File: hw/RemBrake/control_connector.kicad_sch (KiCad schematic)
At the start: 6 parts, among them J4 Conn_01x08_MountingPin, J5 Conn_01x04_MountingPin, J6 Conn_01x03_MountingPin

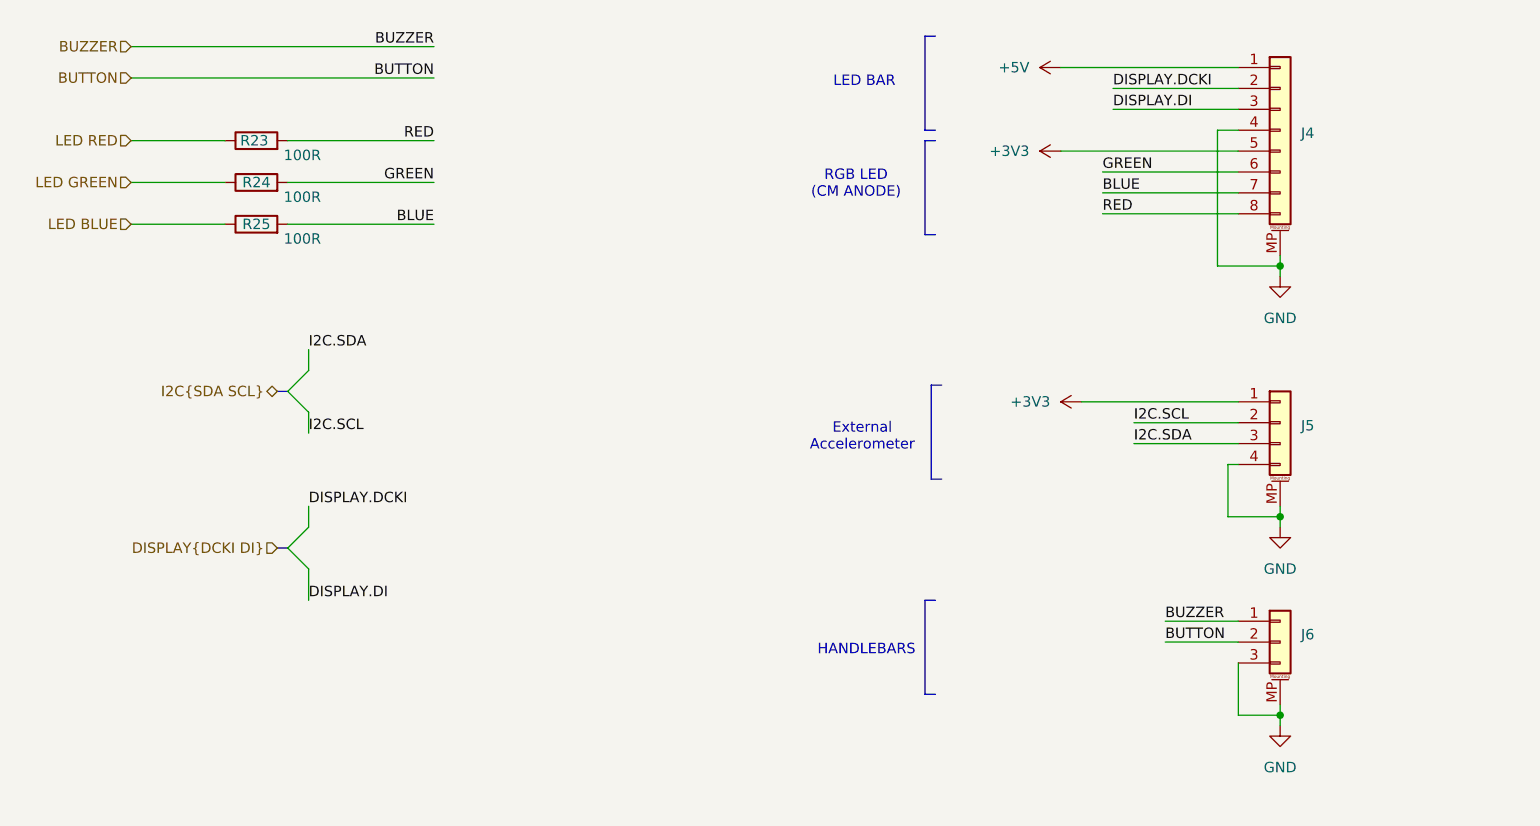
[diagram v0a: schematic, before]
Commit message: added few components to fix indicator LED undefined cathode voltage and added vbus divider to match MCU voltage level
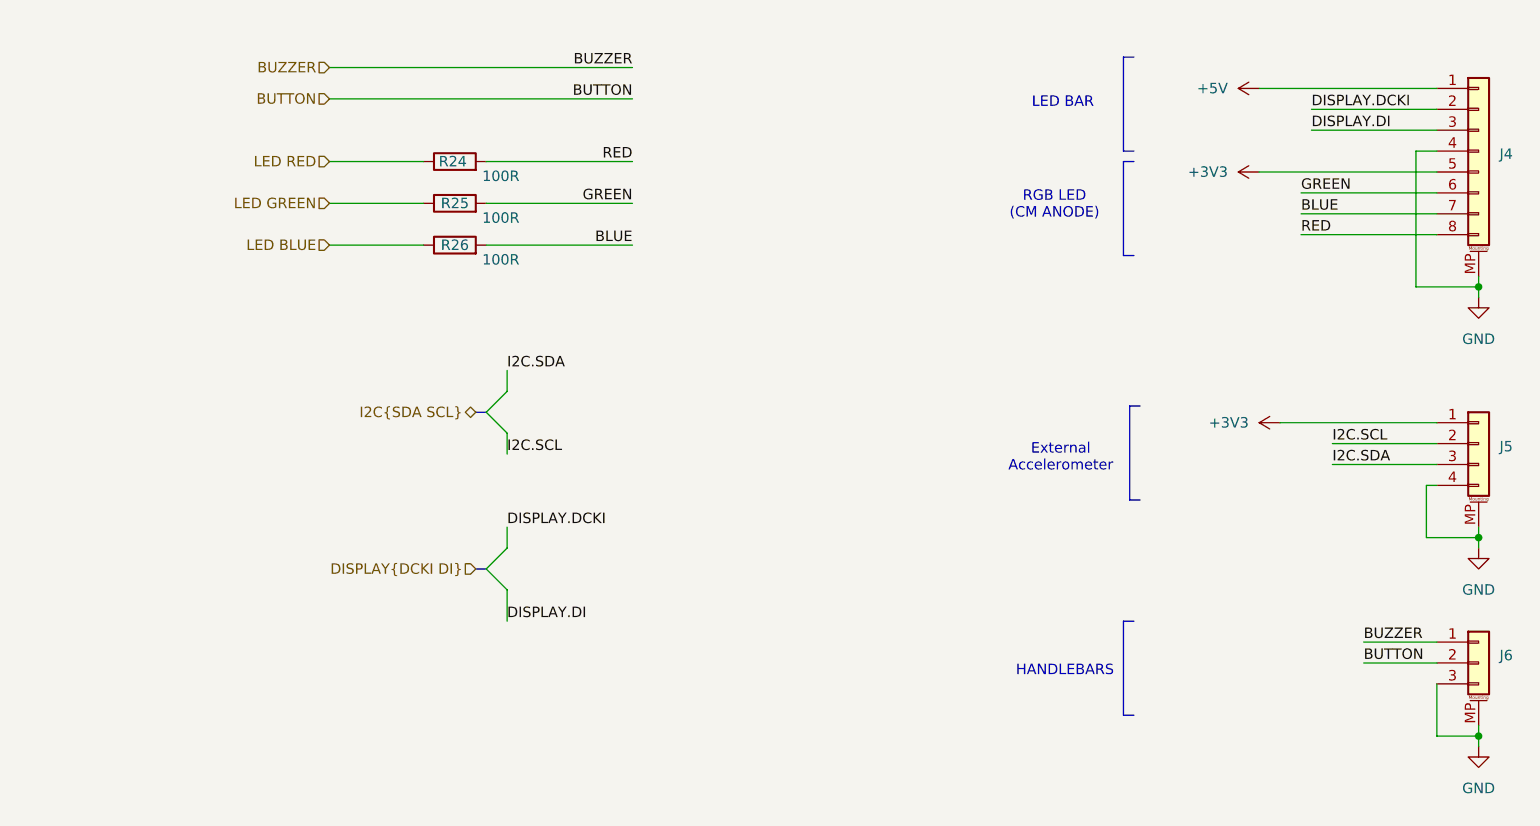
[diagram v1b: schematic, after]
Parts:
- renumbered R23 to R24, R24 to R25, R25 to R26
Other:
- moved on the sheet: J4, J5, J6, R24, R25, R26

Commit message: updated routing yet need to do some small adjustment of the polygon priorities
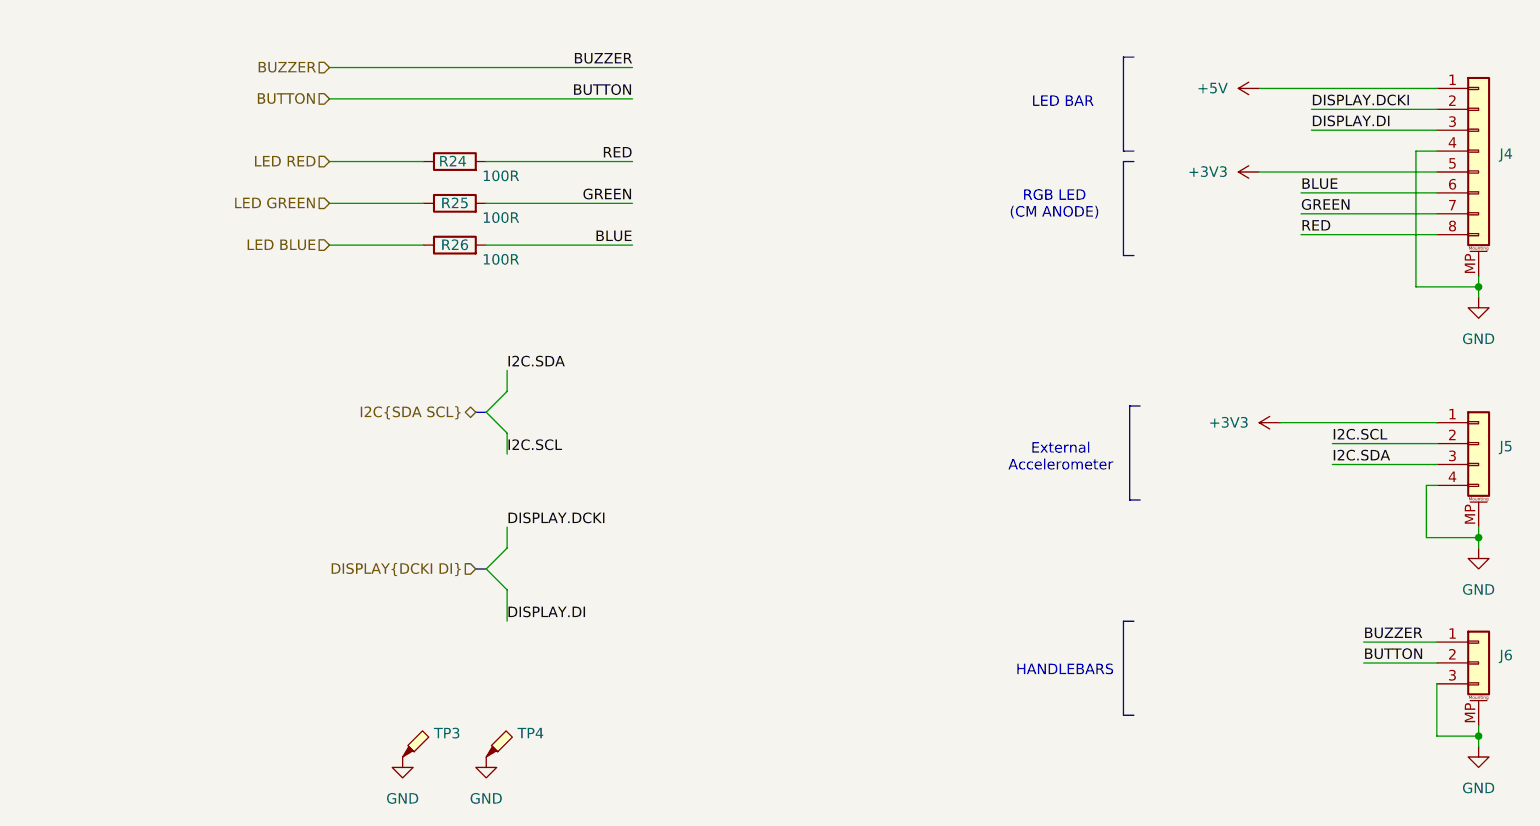
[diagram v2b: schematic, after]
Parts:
- added TP3, TP4: TestPoint_Probe, TestPoint:TestPoint_Pad_1.5x1.5mm, symbol Connector:TestPoint_Probe
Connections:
- net BLUE: now also J4.6 (Pin_6); no longer J4.7 (Pin_7)
- net GND: now also TP3.1, TP4.1
- net GREEN: now also J4.7 (Pin_7); no longer J4.6 (Pin_6)

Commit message: updated date and revision in the schematics
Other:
- company: (none) -> Pacner Bros Tech
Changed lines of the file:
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@@
 	(title_block
 		(title "Control Connector")
-		(date "2024-12-15")
-		(rev "1.0")
+		(date "2025-02-23")
+		(rev "2.0")
+		(company "Pacner Bros Tech")
 	)
 	(text "RGB LED\n(CM ANODE)\n"

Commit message: updated annotation
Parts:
- renumbered R24 to R28, R25 to R29, R26 to R30, TP3 to TP2, TP4 to TP3
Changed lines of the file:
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@@
 		(dnp no)
 		(fields_autoplaced yes)
-		(property "Reference" "#PWR062"
+		(property "Reference" "#PWR027"
 			(at 96.52 146.05 0)
 			(hide yes)
@@
 			(project "RemBrake"
 				(path "/e6d4ae5b-c9d7-4cbe-b288-c929fdf55a75/c6fda42a-9645-46e5-b66a-57cf8664dccf"
-					(reference "#PWR062")
+					(reference "#PWR027")
 					(unit 1)
 				)
@@
 		(on_board yes)
 		(dnp no)
-		(property "Reference" "R24"
+		(property "Reference" "R28"
 			(at 92.456 67.31 90)
 			(effects
@@
 		)
 		(property "Value" "100R"
-			(at 98.298 69.088 90)
+			(at 92.71 69.596 90)
 			(effects
 				(font
@@
 			(project "RemBrake"
 				(path "/e6d4ae5b-c9d7-4cbe-b288-c929fdf55a75/c6fda42a-9645-46e5-b66a-57cf8664dccf"
-					(reference "R24")
+					(reference "R28")
 					(unit 1)
 				)
@@
 		(dnp no)
 		(fields_autoplaced yes)
-		(property "Reference" "#PWR026"
+		(property "Reference" "#PWR030"
 			(at 196.85 99.06 0)
 			(hide yes)
@@
 			(project "RemBrake"
 				(path "/e6d4ae5b-c9d7-4cbe-b288-c929fdf55a75/c6fda42a-9645-46e5-b66a-57cf8664dccf"
-					(reference "#PWR026")
+					(reference "#PWR030")
 					(unit 1)
 				)
@@
 		(on_board yes)
 		(dnp no)
-		(property "Reference" "R25"
+		(property "Reference" "R29"
 			(at 92.71 72.39 90)
 			(effects
@@
 		)
 		(property "Value" "100R"
-			(at 98.298 74.168 90)
+			(at 92.71 74.676 90)
 			(effects
 				(font
@@
 			(project "RemBrake"
 				(path "/e6d4ae5b-c9d7-4cbe-b288-c929fdf55a75/c6fda42a-9645-46e5-b66a-57cf8664dccf"
-					(reference "R25")
+					(reference "R29")
 					(unit 1)
 				)
@@
 		(dnp no)
 		(fields_autoplaced yes)
-		(property "Reference" "#PWR028"
+		(property "Reference" "#PWR032"
 			(at 217.17 120.65 0)
 			(hide yes)
@@
 			(project "RemBrake"
 				(path "/e6d4ae5b-c9d7-4cbe-b288-c929fdf55a75/c6fda42a-9645-46e5-b66a-57cf8664dccf"
-					(reference "#PWR028")
+					(reference "#PWR032")
 					(unit 1)
 				)
@@
 		(dnp no)
 		(fields_autoplaced yes)
-		(property "Reference" "#PWR027"
+		(property "Reference" "#PWR031"
 			(at 217.17 90.17 0)
 			(hide yes)
@@
 			(project "RemBrake"
 				(path "/e6d4ae5b-c9d7-4cbe-b288-c929fdf55a75/c6fda42a-9645-46e5-b66a-57cf8664dccf"
-					(reference "#PWR027")
+					(reference "#PWR031")
 					(unit 1)
 				)
@@
 		(dnp no)
 		(fields_autoplaced yes)
-		(property "Reference" "TP4"
+		(property "Reference" "TP3"
 			(at 100.33 136.8424 0)
 			(effects
@@
 			(project "RemBrake"
 				(path "/e6d4ae5b-c9d7-4cbe-b288-c929fdf55a75/c6fda42a-9645-46e5-b66a-57cf8664dccf"
-					(reference "TP4")
+					(reference "TP3")
 					(unit 1)
 				)
@@
 		(on_board yes)
 		(dnp no)
-		(property "Reference" "R26"
+		(property "Reference" "R30"
 			(at 92.71 77.47 90)
 			(effects
@@
 		)
 		(property "Value" "100R"
-			(at 98.298 79.248 90)
+			(at 92.71 80.01 90)
 			(effects
 				(font
@@
 			(project "RemBrake"
 				(path "/e6d4ae5b-c9d7-4cbe-b288-c929fdf55a75/c6fda42a-9645-46e5-b66a-57cf8664dccf"
-					(reference "R26")
+					(reference "R30")
 					(unit 1)
 				)
@@
 		(dnp no)
 		(fields_autoplaced yes)
-		(property "Reference" "#PWR061"
+		(property "Reference" "#PWR026"
 			(at 86.36 146.05 0)
 			(hide yes)
@@
 			(project "RemBrake"
 				(path "/e6d4ae5b-c9d7-4cbe-b288-c929fdf55a75/c6fda42a-9645-46e5-b66a-57cf8664dccf"
-					(reference "#PWR061")
+					(reference "#PWR026")
 					(unit 1)
 				)
@@
 		(dnp no)
 		(fields_autoplaced yes)
-		(property "Reference" "#PWR029"
+		(property "Reference" "#PWR033"
 			(at 217.17 144.78 0)
 			(hide yes)
@@
 			(project "RemBrake"
 				(path "/e6d4ae5b-c9d7-4cbe-b288-c929fdf55a75/c6fda42a-9645-46e5-b66a-57cf8664dccf"
-					(reference "#PWR029")
+					(reference "#PWR033")
 					(unit 1)
 				)
@@
 		(dnp no)
 		(fields_autoplaced yes)
-		(property "Reference" "#PWR024"
+		(property "Reference" "#PWR028"
 			(at 194.31 58.42 0)
 			(hide yes)
@@
 			(project "RemBrake"
 				(path "/e6d4ae5b-c9d7-4cbe-b288-c929fdf55a75/c6fda42a-9645-46e5-b66a-57cf8664dccf"
-					(reference "#PWR024")
+					(reference "#PWR028")
 					(unit 1)
 				)
@@
 		(dnp no)
 		(fields_autoplaced yes)
-		(property "Reference" "TP3"
+		(property "Reference" "TP2"
 			(at 90.17 136.8424 0)
 			(effects
@@
 			(project "RemBrake"
 				(path "/e6d4ae5b-c9d7-4cbe-b288-c929fdf55a75/c6fda42a-9645-46e5-b66a-57cf8664dccf"
-					(reference "TP3")
+					(reference "TP2")
 					(unit 1)
 				)
@@
 		(dnp no)
 		(fields_autoplaced yes)
-		(property "Reference" "#PWR025"
+		(property "Reference" "#PWR029"
 			(at 194.31 68.58 0)
 			(hide yes)
@@
 			(project "RemBrake"
 				(path "/e6d4ae5b-c9d7-4cbe-b288-c929fdf55a75/c6fda42a-9645-46e5-b66a-57cf8664dccf"
-					(reference "#PWR025")
-					(unit 1)
-				)
+					(reference "#PWR029")
+					(unit 1)
+				)

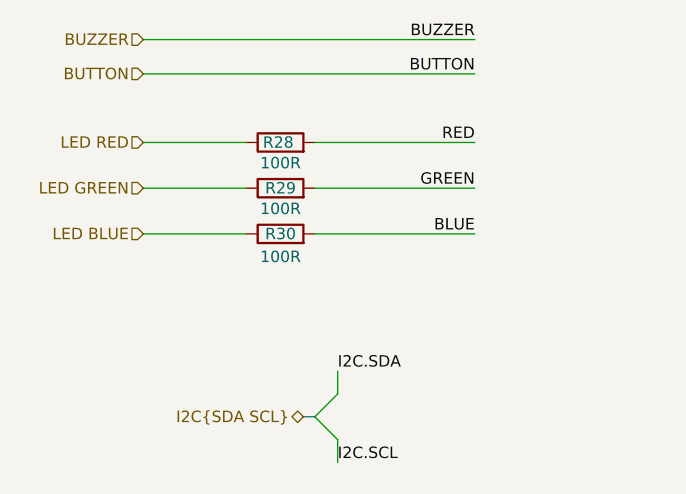
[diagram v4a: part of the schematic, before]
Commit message: fixed bugs with LED reverse current leakage and beeper deterministic startup delay
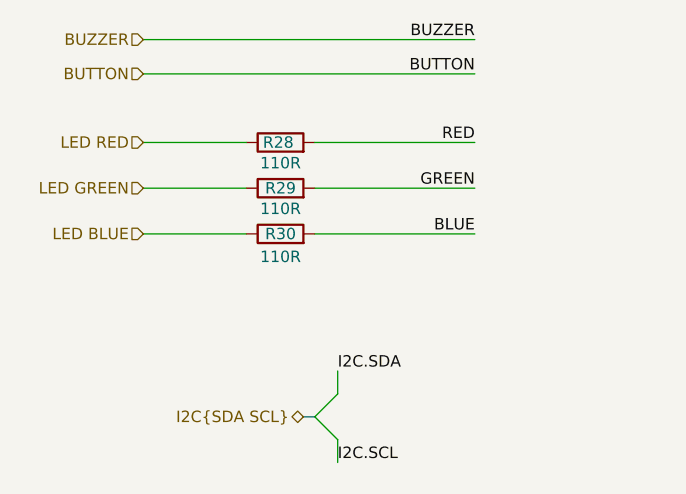
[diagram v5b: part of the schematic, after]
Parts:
- R28, R29, R30: value 100R -> 110R
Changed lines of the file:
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@@
 (kicad_sch
-	(version 20250114)
+	(version 20250222)
 	(generator "eeschema")
 	(generator_version "9.99")
@@
 			)
 		)
-		(property "Value" "100R"
+		(property "Value" "110R"
 			(at 92.71 69.596 90)
 			(effects
@@
 			)
 		)
-		(property "Value" "100R"
+		(property "Value" "110R"
 			(at 92.71 74.676 90)
 			(effects
@@
 			)
 		)
-		(property "Value" "100R"
+		(property "Value" "110R"
 			(at 92.71 80.01 90)
 			(effects

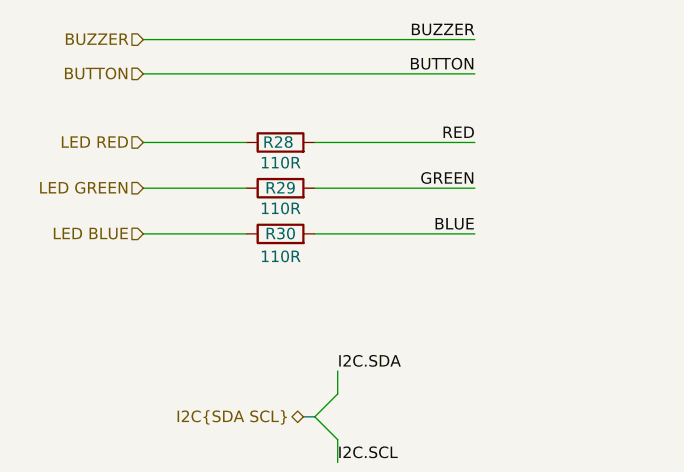
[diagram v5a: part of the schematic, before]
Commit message: replaced optocoupler with transistor and loaded components in the pcb sheet
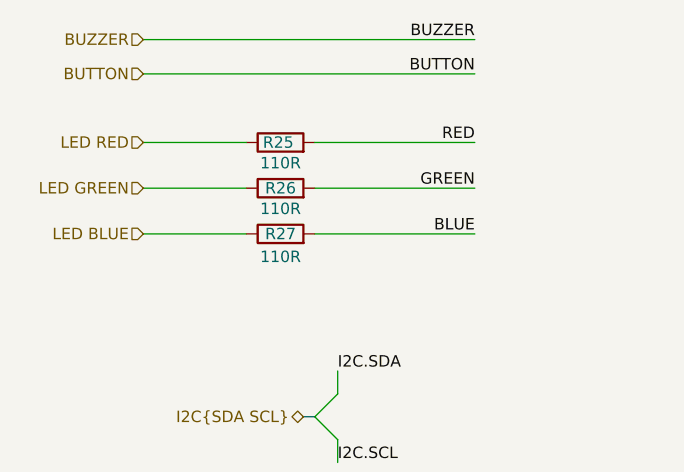
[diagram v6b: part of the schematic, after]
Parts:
- renumbered R28 to R25, R29 to R26, R30 to R27
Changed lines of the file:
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@@
 (kicad_sch
-	(version 20250222)
+	(version 20250227)
 	(generator "eeschema")
 	(generator_version "9.99")
@@
 		(dnp no)
 		(fields_autoplaced yes)
-		(property "Reference" "#PWR027"
+		(property "Reference" "#PWR026"
 			(at 96.52 146.05 0)
 			(hide yes)
@@
 			(project "RemBrake"
 				(path "/e6d4ae5b-c9d7-4cbe-b288-c929fdf55a75/c6fda42a-9645-46e5-b66a-57cf8664dccf"
-					(reference "#PWR027")
+					(reference "#PWR026")
 					(unit 1)
 				)
@@
 		(on_board yes)
 		(dnp no)
-		(property "Reference" "R28"
+		(property "Reference" "R25"
 			(at 92.456 67.31 90)
 			(effects
@@
 			(project "RemBrake"
 				(path "/e6d4ae5b-c9d7-4cbe-b288-c929fdf55a75/c6fda42a-9645-46e5-b66a-57cf8664dccf"
-					(reference "R28")
+					(reference "R25")
 					(unit 1)
 				)
@@
 		(dnp no)
 		(fields_autoplaced yes)
-		(property "Reference" "#PWR030"
+		(property "Reference" "#PWR029"
 			(at 196.85 99.06 0)
 			(hide yes)
@@
 			(project "RemBrake"
 				(path "/e6d4ae5b-c9d7-4cbe-b288-c929fdf55a75/c6fda42a-9645-46e5-b66a-57cf8664dccf"
-					(reference "#PWR030")
+					(reference "#PWR029")
 					(unit 1)
 				)
@@
 		(on_board yes)
 		(dnp no)
-		(property "Reference" "R29"
+		(property "Reference" "R26"
 			(at 92.71 72.39 90)
 			(effects
@@
 			(project "RemBrake"
 				(path "/e6d4ae5b-c9d7-4cbe-b288-c929fdf55a75/c6fda42a-9645-46e5-b66a-57cf8664dccf"
-					(reference "R29")
+					(reference "R26")
 					(unit 1)
 				)
@@
 		(dnp no)
 		(fields_autoplaced yes)
-		(property "Reference" "#PWR032"
+		(property "Reference" "#PWR031"
 			(at 217.17 120.65 0)
 			(hide yes)
@@
 			(project "RemBrake"
 				(path "/e6d4ae5b-c9d7-4cbe-b288-c929fdf55a75/c6fda42a-9645-46e5-b66a-57cf8664dccf"
-					(reference "#PWR032")
+					(reference "#PWR031")
 					(unit 1)
 				)
@@
 		(dnp no)
 		(fields_autoplaced yes)
-		(property "Reference" "#PWR031"
+		(property "Reference" "#PWR030"
 			(at 217.17 90.17 0)
 			(hide yes)
@@
 			(project "RemBrake"
 				(path "/e6d4ae5b-c9d7-4cbe-b288-c929fdf55a75/c6fda42a-9645-46e5-b66a-57cf8664dccf"
-					(reference "#PWR031")
+					(reference "#PWR030")
 					(unit 1)
 				)
@@
 		(on_board yes)
 		(dnp no)
-		(property "Reference" "R30"
+		(property "Reference" "R27"
 			(at 92.71 77.47 90)
 			(effects
@@
 			(project "RemBrake"
 				(path "/e6d4ae5b-c9d7-4cbe-b288-c929fdf55a75/c6fda42a-9645-46e5-b66a-57cf8664dccf"
-					(reference "R30")
+					(reference "R27")
 					(unit 1)
 				)
@@
 		(dnp no)
 		(fields_autoplaced yes)
-		(property "Reference" "#PWR026"
+		(property "Reference" "#PWR025"
 			(at 86.36 146.05 0)
 			(hide yes)
@@
 			(project "RemBrake"
 				(path "/e6d4ae5b-c9d7-4cbe-b288-c929fdf55a75/c6fda42a-9645-46e5-b66a-57cf8664dccf"
-					(reference "#PWR026")
+					(reference "#PWR025")
 					(unit 1)
 				)
@@
 		(dnp no)
 		(fields_autoplaced yes)
-		(property "Reference" "#PWR033"
+		(property "Reference" "#PWR032"
 			(at 217.17 144.78 0)
 			(hide yes)
@@
 			(project "RemBrake"
 				(path "/e6d4ae5b-c9d7-4cbe-b288-c929fdf55a75/c6fda42a-9645-46e5-b66a-57cf8664dccf"
-					(reference "#PWR033")
+					(reference "#PWR032")
 					(unit 1)
 				)
@@
 		(dnp no)
 		(fields_autoplaced yes)
-		(property "Reference" "#PWR028"
+		(property "Reference" "#PWR027"
 			(at 194.31 58.42 0)
 			(hide yes)
@@
 			(project "RemBrake"
 				(path "/e6d4ae5b-c9d7-4cbe-b288-c929fdf55a75/c6fda42a-9645-46e5-b66a-57cf8664dccf"
-					(reference "#PWR028")
+					(reference "#PWR027")
 					(unit 1)
 				)
@@
 		(dnp no)
 		(fields_autoplaced yes)
-		(property "Reference" "#PWR029"
+		(property "Reference" "#PWR028"
 			(at 194.31 68.58 0)
 			(hide yes)
@@
 			(project "RemBrake"
 				(path "/e6d4ae5b-c9d7-4cbe-b288-c929fdf55a75/c6fda42a-9645-46e5-b66a-57cf8664dccf"
-					(reference "#PWR029")
+					(reference "#PWR028")
 					(unit 1)
 				)
